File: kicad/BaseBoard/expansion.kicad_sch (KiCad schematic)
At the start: 9 parts, among them J4 Control and Data, J5 Address Bus, J6 Chip Selects, J7 PA/PB, J8 Power, J9 Power, U9 W65C22NxP

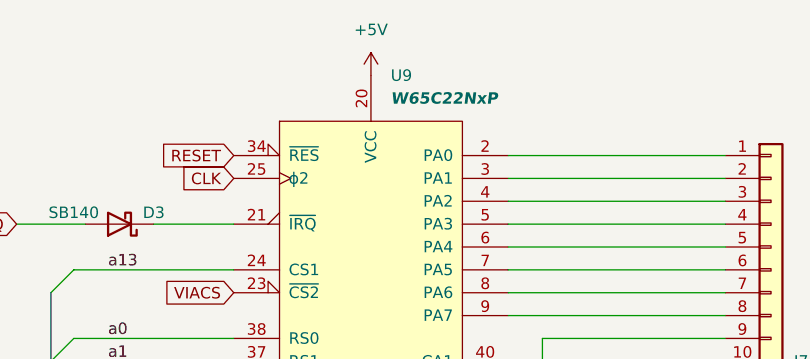
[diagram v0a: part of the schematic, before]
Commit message: I/O board schematic and layout
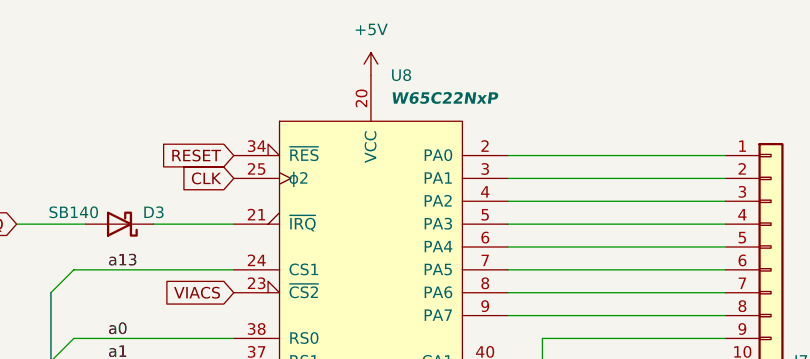
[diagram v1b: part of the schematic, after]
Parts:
- renumbered U9 to U8
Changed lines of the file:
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@@
   (symbol (lib_id "power:GND") (at 259.08 86.36 0) (unit 1)
     (in_bom yes) (on_board yes) (dnp no) (fields_autoplaced)
-    (property "Reference" "#PWR058" (at 259.08 92.71 0)
+    (property "Reference" "#PWR056" (at 259.08 92.71 0)
       (effects (font (size 1.27 1.27)) hide)
     )
@@
       (project "MiniComputerBase"
         (path "/3f118084-1458-40be-b12b-e8391c9e712b/ba62a70e-9bd1-4f2a-b61d-377ee8ac92c8"
-          (reference "#PWR058") (unit 1)
+          (reference "#PWR056") (unit 1)
         )
       )
@@
   (symbol (lib_id "power:+5V") (at 144.78 25.4 0) (unit 1)
     (in_bom yes) (on_board yes) (dnp no) (fields_autoplaced)
-    (property "Reference" "#PWR053" (at 144.78 29.21 0)
+    (property "Reference" "#PWR051" (at 144.78 29.21 0)
       (effects (font (size 1.27 1.27)) hide)
     )
@@
       (project "MiniComputerBase"
         (path "/3f118084-1458-40be-b12b-e8391c9e712b/ba62a70e-9bd1-4f2a-b61d-377ee8ac92c8"
-          (reference "#PWR053") (unit 1)
+          (reference "#PWR051") (unit 1)
         )
       )
@@
   (symbol (lib_id "power:GND") (at 144.78 99.06 0) (unit 1)
     (in_bom yes) (on_board yes) (dnp no) (fields_autoplaced)
-    (property "Reference" "#PWR054" (at 144.78 105.41 0)
+    (property "Reference" "#PWR052" (at 144.78 105.41 0)
       (effects (font (size 1.27 1.27)) hide)
     )
@@
       (project "MiniComputerBase"
         (path "/3f118084-1458-40be-b12b-e8391c9e712b/ba62a70e-9bd1-4f2a-b61d-377ee8ac92c8"
-          (reference "#PWR054") (unit 1)
+          (reference "#PWR052") (unit 1)
         )
       )
@@
   (symbol (lib_id "power:VDD") (at 259.08 102.87 0) (unit 1)
     (in_bom yes) (on_board yes) (dnp no) (fields_autoplaced)
-    (property "Reference" "#PWR059" (at 259.08 106.68 0)
+    (property "Reference" "#PWR057" (at 259.08 106.68 0)
       (effects (font (size 1.27 1.27)) hide)
     )
@@
       (project "MiniComputerBase"
         (path "/3f118084-1458-40be-b12b-e8391c9e712b/ba62a70e-9bd1-4f2a-b61d-377ee8ac92c8"
-          (reference "#PWR059") (unit 1)
+          (reference "#PWR057") (unit 1)
         )
       )
@@
   (symbol (lib_id "power:GND") (at 260.35 118.11 0) (unit 1)
     (in_bom yes) (on_board yes) (dnp no) (fields_autoplaced)
-    (property "Reference" "#PWR060" (at 260.35 124.46 0)
+    (property "Reference" "#PWR058" (at 260.35 124.46 0)
       (effects (font (size 1.27 1.27)) hide)
     )
@@
       (project "MiniComputerBase"
         (path "/3f118084-1458-40be-b12b-e8391c9e712b/ba62a70e-9bd1-4f2a-b61d-377ee8ac92c8"
-          (reference "#PWR060") (unit 1)
+          (reference "#PWR058") (unit 1)
         )
       )
@@
   (symbol (lib_id "MOS6502:W65C22NxP") (at 144.78 62.23 0) (unit 1)
     (in_bom yes) (on_board yes) (dnp no) (fields_autoplaced)
-    (property "Reference" "U9" (at 146.9741 25.4 0)
+    (property "Reference" "U8" (at 146.9741 25.4 0)
       (effects (font (size 1.27 1.27)) (justify left))
     )
@@
       (project "MiniComputerBase"
         (path "/3f118084-1458-40be-b12b-e8391c9e712b/ba62a70e-9bd1-4f2a-b61d-377ee8ac92c8"
-          (reference "U9") (unit 1)
+          (reference "U8") (unit 1)
         )
       )
@@
   (symbol (lib_id "power:+3V3") (at 273.05 113.03 0) (unit 1)
     (in_bom yes) (on_board yes) (dnp no) (fields_autoplaced)
-    (property "Reference" "#PWR064" (at 273.05 116.84 0)
+    (property "Reference" "#PWR062" (at 273.05 116.84 0)
       (effects (font (size 1.27 1.27)) hide)
     )
@@
       (project "MiniComputerBase"
         (path "/3f118084-1458-40be-b12b-e8391c9e712b/ba62a70e-9bd1-4f2a-b61d-377ee8ac92c8"
-          (reference "#PWR064") (unit 1)
+          (reference "#PWR062") (unit 1)
         )
       )
@@
   (symbol (lib_id "power:+5V") (at 265.43 76.2 0) (unit 1)
     (in_bom yes) (on_board yes) (dnp no) (fields_autoplaced)
-    (property "Reference" "#PWR061" (at 265.43 80.01 0)
+    (property "Reference" "#PWR059" (at 265.43 80.01 0)
       (effects (font (size 1.27 1.27)) hide)
     )
@@
       (project "MiniComputerBase"
         (path "/3f118084-1458-40be-b12b-e8391c9e712b/ba62a70e-9bd1-4f2a-b61d-377ee8ac92c8"
-          (reference "#PWR061") (unit 1)
+          (reference "#PWR059") (unit 1)
         )
       )
@@
   (symbol (lib_id "power:+3V3") (at 271.78 81.28 0) (unit 1)
     (in_bom yes) (on_board yes) (dnp no) (fields_autoplaced)
-    (property "Reference" "#PWR063" (at 271.78 85.09 0)
+    (property "Reference" "#PWR061" (at 271.78 85.09 0)
       (effects (font (size 1.27 1.27)) hide)
     )
@@
       (project "MiniComputerBase"
         (path "/3f118084-1458-40be-b12b-e8391c9e712b/ba62a70e-9bd1-4f2a-b61d-377ee8ac92c8"
-          (reference "#PWR063") (unit 1)
+          (reference "#PWR061") (unit 1)
         )
       )
@@
         )
         (path "/3f118084-1458-40be-b12b-e8391c9e712b/ba62a70e-9bd1-4f2a-b61d-377ee8ac92c8"
-          (reference "#PWR055") (unit 1)
+          (reference "#PWR053") (unit 1)
         )
       )
@@
   (symbol (lib_id "power:VDD") (at 257.81 71.12 0) (unit 1)
     (in_bom yes) (on_board yes) (dnp no) (fields_autoplaced)
-    (property "Reference" "#PWR057" (at 257.81 74.93 0)
+    (property "Reference" "#PWR055" (at 257.81 74.93 0)
       (effects (font (size 1.27 1.27)) hide)
     )
@@
       (project "MiniComputerBase"
         (path "/3f118084-1458-40be-b12b-e8391c9e712b/ba62a70e-9bd1-4f2a-b61d-377ee8ac92c8"
-          (reference "#PWR057") (unit 1)
+          (reference "#PWR055") (unit 1)
         )
       )
@@
   (symbol (lib_id "power:+5V") (at 266.7 107.95 0) (unit 1)
     (in_bom yes) (on_board yes) (dnp no) (fields_autoplaced)
-    (property "Reference" "#PWR062" (at 266.7 111.76 0)
+    (property "Reference" "#PWR060" (at 266.7 111.76 0)
       (effects (font (size 1.27 1.27)) hide)
     )
@@
       (project "MiniComputerBase"
         (path "/3f118084-1458-40be-b12b-e8391c9e712b/ba62a70e-9bd1-4f2a-b61d-377ee8ac92c8"
-          (reference "#PWR062") (unit 1)
+          (reference "#PWR060") (unit 1)
         )
       )
@@
         )
         (path "/3f118084-1458-40be-b12b-e8391c9e712b/ba62a70e-9bd1-4f2a-b61d-377ee8ac92c8"
-          (reference "#PWR056") (unit 1)
-        )
-      )
+          (reference "#PWR054") (unit 1)
+        )
+      )
